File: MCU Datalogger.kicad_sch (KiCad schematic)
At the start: 25 parts, among them U1 24LC1025, U2 24LC1025, U3 ATMEGA328P-AU, U4 DS1337S_, Y1 Crystal, Y2 Crystal

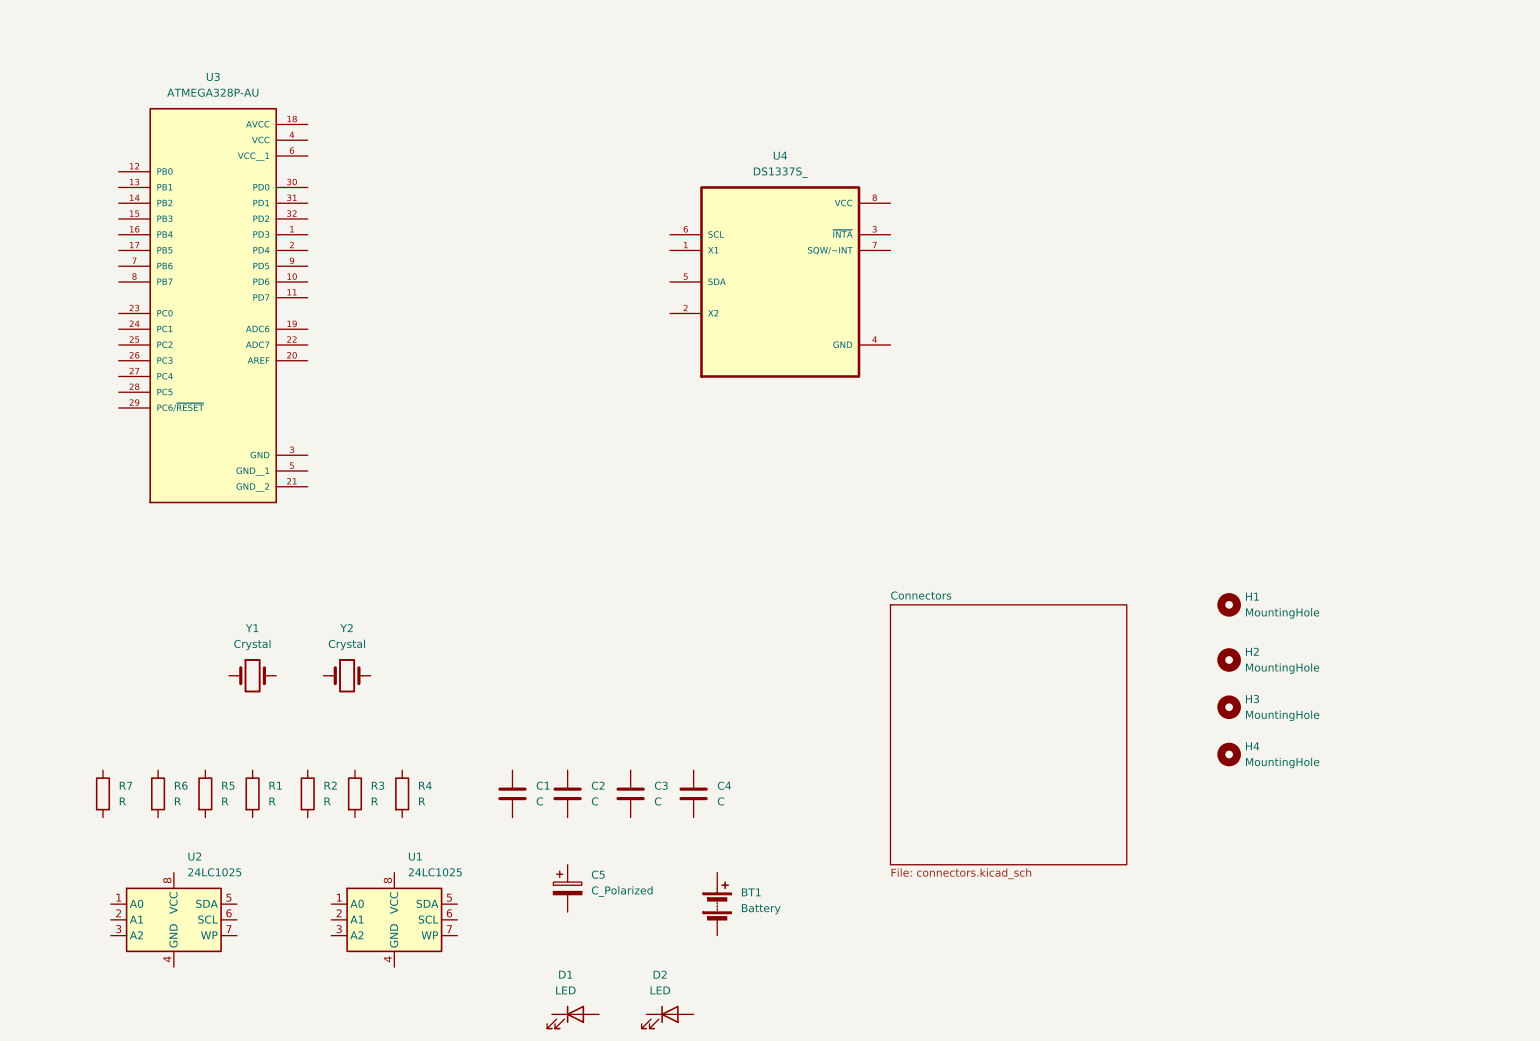
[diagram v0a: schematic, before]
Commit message: changed location of components
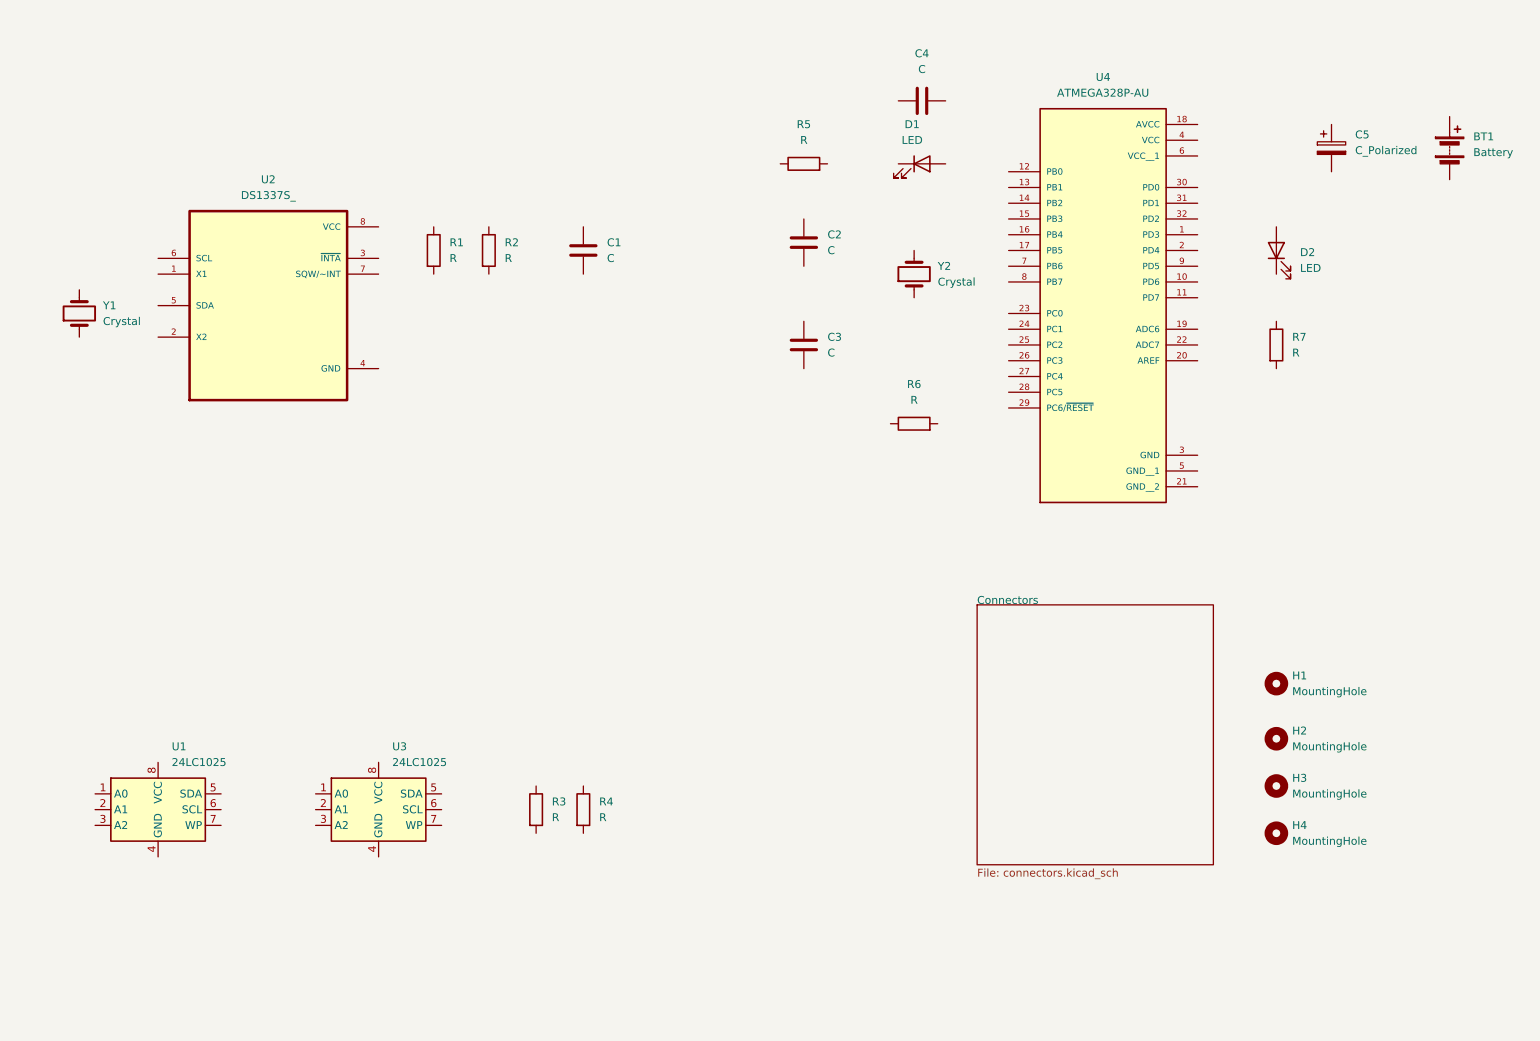
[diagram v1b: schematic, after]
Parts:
- renumbered R6 to R3, R5 to R4, R3 to R5, R7 to R6, R4 to R7, U2 to U1, U4 to U2, U1 to U3, U3 to U4
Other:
- moved on the sheet: BT1, C1, C2, C3, C4, C5, D1, D2, H1, H2, H3, H4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

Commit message: added component values
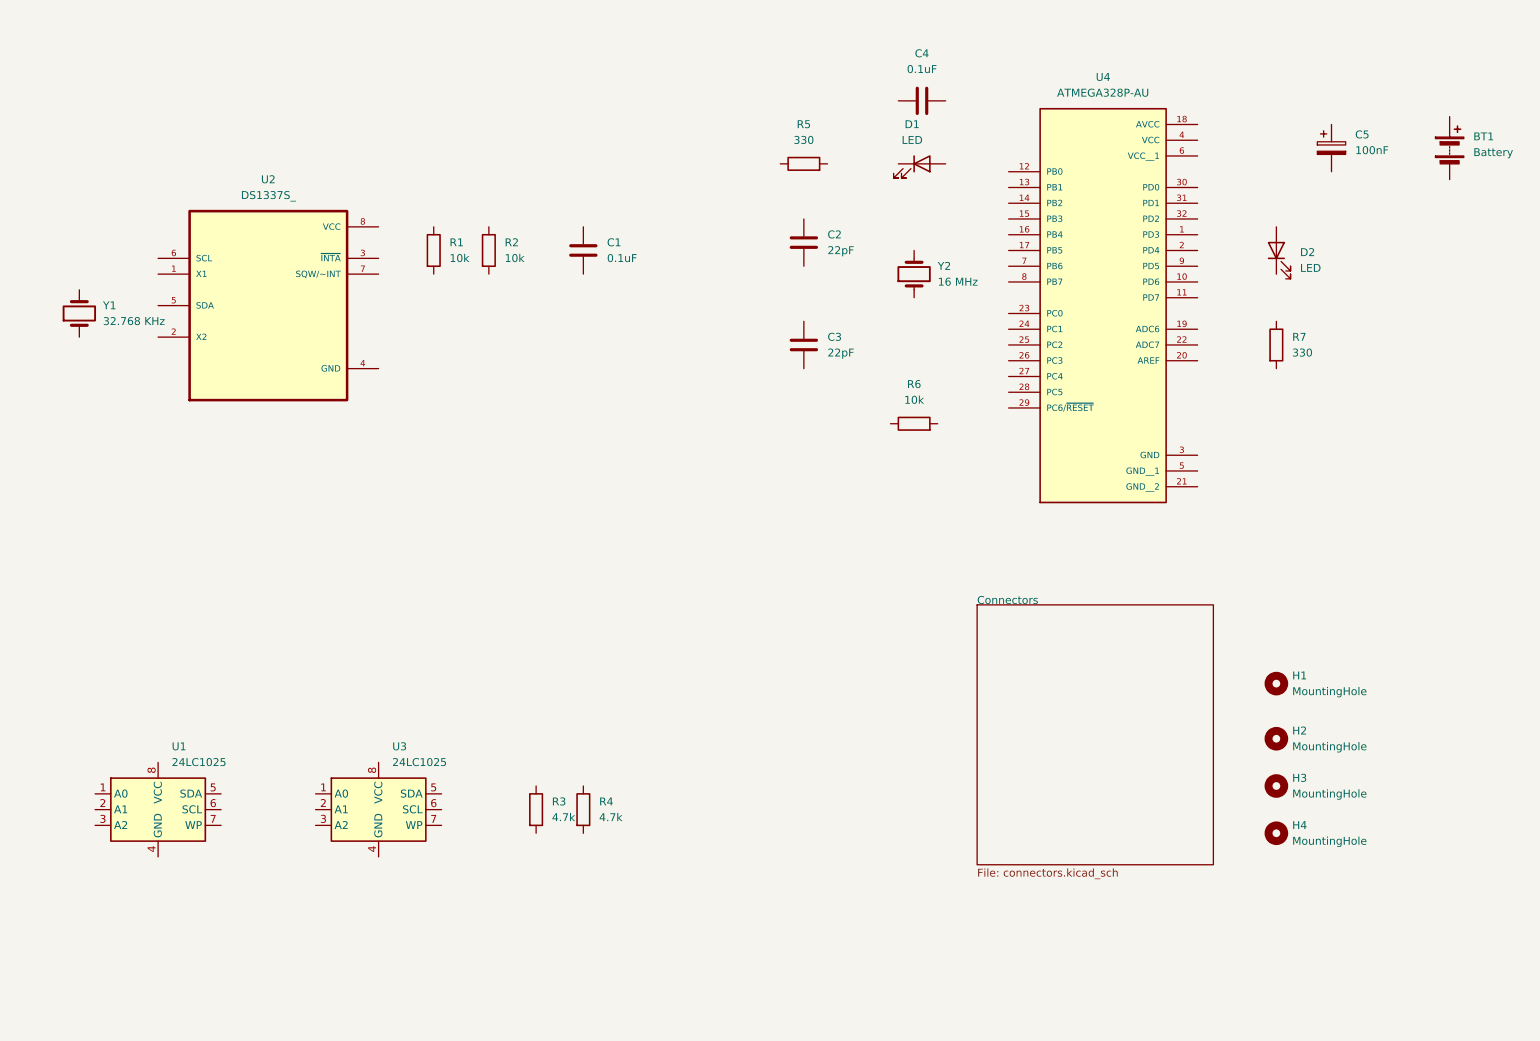
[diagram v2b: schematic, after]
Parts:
- C1, C4: value C -> 0.1uF
- C2, C3: value C -> 22pF
- C5: value C_Polarized -> 100nF
- R1, R2, R6: value R -> 10k
- R3, R4: value R -> 4.7k
- R5, R7: value R -> 330
- Y1: value Crystal -> 32.768 KHz
- Y2: value Crystal -> 16 MHz
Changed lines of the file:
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@@
 			)
 		)
-		(property "Value" "C"
+		(property "Value" "22pF"
 			(at 160.02 73.6599 0)
 			(effects
@@
 			)
 		)
-		(property "Value" "C"
+		(property "Value" "0.1uF"
 			(at 124.46 58.4199 0)
 			(effects
@@
 			)
 		)
-		(property "Value" "Crystal"
+		(property "Value" "32.768 KHz"
 			(at 43.18 68.5799 90)
 			(effects
@@
 			)
 		)
+		(property "Purpose" ""
+			(at 39.37 67.31 0)
+			(effects
+				(font
+					(size 1.27 1.27)
+				)
+				(hide yes)
+			)
+		)
 		(pin "2"
 		)
@@
 			)
 		)
-		(property "Value" "R"
+		(property "Value" "330"
 			(at 156.21 39.37 90)
 			(effects
@@
 			)
 		)
+		(property "Purpose" ""
+			(at 156.21 43.18 0)
+			(effects
+				(font
+					(size 1.27 1.27)
+				)
+				(hide yes)
+			)
+		)
 		(pin "2"
 		)
@@
 			)
 		)
-		(property "Value" "R"
+		(property "Value" "330"
 			(at 234.95 73.6599 0)
 			(effects
@@
 			)
 		)
-		(property "Value" "R"
+		(property "Value" "10k"
 			(at 107.95 58.4199 0)
 			(effects
@@
 			)
 		)
-		(property "Value" "C_Polarized"
+		(property "Value" "100nF"
 			(at 245.11 41.0209 0)
 			(effects
@@
 			)
 		)
-		(property "Value" "R"
+		(property "Value" "10k"
 			(at 99.06 58.4199 0)
 			(effects
@@
 			)
 		)
+		(property "Purpose" ""
+			(at 96.52 57.15 0)
+			(effects
+				(font
+					(size 1.27 1.27)
+				)
+				(hide yes)
+			)
+		)
 		(pin "2"
 		)
@@
 			)
 		)
-		(property "Value" "R"
+		(property "Value" "4.7k"
 			(at 115.57 148.5899 0)
 			(effects
@@
 			)
 		)
-		(property "Value" "R"
+		(property "Value" "4.7k"
 			(at 123.19 148.5899 0)
 			(effects
@@
 			)
 		)
-		(property "Value" "R"
+		(property "Value" "10k"
 			(at 173.99 81.28 90)
 			(effects
@@
 			)
 		)
-		(property "Value" "C"
+		(property "Value" "0.1uF"
 			(at 175.26 27.94 90)
 			(effects
@@
 			)
 		)
+		(property "Purpose" ""
+			(at 175.26 33.02 0)
+			(effects
+				(font
+					(size 1.27 1.27)
+				)
+				(hide yes)
+			)
+		)
 		(pin "2"
 		)
@@
 			)
 		)
-		(property "Value" "C"
+		(property "Value" "22pF"
 			(at 160.02 57.1499 0)
 			(effects
@@
 			)
 		)
-		(property "Value" "Crystal"
+		(property "Value" "16 MHz"
 			(at 177.8 62.2299 90)
 			(effects

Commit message: Added 3rd party footprints
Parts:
- BT1: footprint (none) -> Connector_PinHeader_1.00mm:PinHeader_1x02_P1.00mm_Vertical
- C1, C2, C3, C4, C5: footprint (none) -> Capacitor_SMD:C_0805_2012Metric_Pad1.18x1.45mm_HandSolder
- D1, D2: footprint (none) -> LED_SMD:LED_0805_2012Metric_Pad1.15x1.40mm_HandSolder
- H1, H2, H3, H4: footprint (none) -> MountingHole:MountingHole_2.1mm
- R1, R2, R3, R4, R5, R6, R7: footprint (none) -> Resistor_SMD:R_0805_2012Metric_Pad1.20x1.40mm_HandSolder
- U1, U3: footprint (none) -> Package_SO:SOIC-8_5.23x5.23mm_P1.27mm
- U2: footprint DS1337S_:SOIC127P600X175-8N -> footprints:SOIC127P600X175-8N
- U4: footprint ATMEGA328P-AU:QFP80P900X900X120-32N -> footprints:QFP80P900X900X120-32N
- Y1, Y2: footprint (none) -> Crystal:Crystal_SMD_5032-2Pin_5.0x3.2mm_HandSoldering
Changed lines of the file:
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@@
 			)
 		)
-		(property "Footprint" ""
+		(property "Footprint" "Capacitor_SMD:C_0805_2012Metric_Pad1.18x1.45mm_HandSolder"
 			(at 157.1752 76.2 0)
 			(effects
@@
 			)
 		)
-		(property "Footprint" ""
+		(property "Footprint" "Package_SO:SOIC-8_5.23x5.23mm_P1.27mm"
 			(at 87.63 147.32 0)
 			(effects
@@
 			)
 		)
-		(property "Footprint" ""
+		(property "Footprint" "Connector_PinHeader_1.00mm:PinHeader_1x02_P1.00mm_Vertical"
 			(at 260.35 39.116 90)
 			(effects
@@
 			)
 		)
-		(property "Footprint" ""
+		(property "Footprint" "MountingHole:MountingHole_2.1mm"
 			(at 232.41 135.89 0)
 			(effects
@@
 			)
 		)
-		(property "Footprint" ""
+		(property "Footprint" "MountingHole:MountingHole_2.1mm"
 			(at 232.41 127 0)
 			(effects
@@
 			)
 		)
-		(property "Footprint" ""
+		(property "Footprint" "Capacitor_SMD:C_0805_2012Metric_Pad1.18x1.45mm_HandSolder"
 			(at 121.6152 60.96 0)
 			(effects
@@
 			)
 		)
-		(property "Footprint" ""
+		(property "Footprint" "Crystal:Crystal_SMD_5032-2Pin_5.0x3.2mm_HandSoldering"
 			(at 39.37 67.31 0)
 			(effects
@@
 			)
 		)
-		(property "Footprint" ""
+		(property "Footprint" "Resistor_SMD:R_0805_2012Metric_Pad1.20x1.40mm_HandSolder"
 			(at 156.21 44.958 90)
 			(effects
@@
 			)
 		)
-		(property "Footprint" ""
+		(property "Footprint" "Resistor_SMD:R_0805_2012Metric_Pad1.20x1.40mm_HandSolder"
 			(at 230.632 72.39 90)
 			(effects
@@
 			)
 		)
-		(property "Footprint" ""
+		(property "Footprint" "Resistor_SMD:R_0805_2012Metric_Pad1.20x1.40mm_HandSolder"
 			(at 103.632 57.15 90)
 			(effects
@@
 			)
 		)
-		(property "Footprint" ""
+		(property "Footprint" "Capacitor_SMD:C_0805_2012Metric_Pad1.18x1.45mm_HandSolder"
 			(at 242.2652 44.45 0)
 			(effects
@@
 			)
 		)
-		(property "Footprint" ""
+		(property "Footprint" "Resistor_SMD:R_0805_2012Metric_Pad1.20x1.40mm_HandSolder"
 			(at 94.742 57.15 90)
 			(effects
@@
 			)
 		)
-		(property "Footprint" ""
+		(property "Footprint" "Resistor_SMD:R_0805_2012Metric_Pad1.20x1.40mm_HandSolder"
 			(at 111.252 147.32 90)
 			(effects
@@
 			)
 		)
-		(property "Footprint" ""
+		(property "Footprint" "Resistor_SMD:R_0805_2012Metric_Pad1.20x1.40mm_HandSolder"
 			(at 118.872 147.32 90)
 			(effects
@@
 			)
 		)
-		(property "Footprint" ""
+		(property "Footprint" "MountingHole:MountingHole_2.1mm"
 			(at 232.41 151.13 0)
 			(effects
@@
 			)
 		)
-		(property "Footprint" ""
+		(property "Footprint" "Resistor_SMD:R_0805_2012Metric_Pad1.20x1.40mm_HandSolder"
 			(at 173.99 86.868 90)
 			(effects
@@
 			)
 		)
-		(property "Footprint" ""
+		(property "Footprint" "LED_SMD:LED_0805_2012Metric_Pad1.15x1.40mm_HandSolder"
 			(at 232.41 57.15 0)
 			(effects
@@
 			)
 		)
-		(property "Footprint" ""
+		(property "Footprint" "Capacitor_SMD:C_0805_2012Metric_Pad1.18x1.45mm_HandSolder"
 			(at 179.07 32.0548 0)
 			(effects
@@
 			)
 		)
-		(property "Footprint" ""
+		(property "Footprint" "Package_SO:SOIC-8_5.23x5.23mm_P1.27mm"
 			(at 52.07 147.32 0)
 			(effects
@@
 			)
 		)
-		(property "Footprint" ""
+		(property "Footprint" "LED_SMD:LED_0805_2012Metric_Pad1.15x1.40mm_HandSolder"
 			(at 175.26 43.18 0)
 			(effects
@@
 			)
 		)
-		(property "Footprint" ""
+		(property "Footprint" "MountingHole:MountingHole_2.1mm"
 			(at 232.41 143.51 0)
 			(effects
@@
 			)
 		)
-		(property "Footprint" "DS1337S_:SOIC127P600X175-8N"
+		(property "Footprint" "footprints:SOIC127P600X175-8N"
 			(at 69.85 66.04 0)
 			(effects
@@
 			)
 		)
-		(property "Footprint" ""
+		(property "Footprint" "Capacitor_SMD:C_0805_2012Metric_Pad1.18x1.45mm_HandSolder"
 			(at 157.1752 59.69 0)
 			(effects
@@
 			)
 		)
-		(property "Footprint" "ATMEGA328P-AU:QFP80P900X900X120-32N"
+		(property "Footprint" "footprints:QFP80P900X900X120-32N"
 			(at 204.47 62.23 0)
 			(effects
@@
 			)
 		)
-		(property "Footprint" ""
+		(property "Footprint" "Crystal:Crystal_SMD_5032-2Pin_5.0x3.2mm_HandSoldering"
 			(at 173.99 60.96 0)
 			(effects

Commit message: Wired the main schematic
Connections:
- net GND: now reaches C3.1
- net GND: now also BT1.2 (-), C1.2, C2.1, C4.2, C5.2, R5.1, R7.2, U1.4 (GND), U1.7 (WP), U2.4 (GND), U3.2 (A1), U3.4 (GND), U3.7 (WP), U4.21 (GND__2), U4.3 (GND), U4.5 (GND__1)
- net at C3.2: now also U4.8 (PB7), Y2.1
- net Vcc: now reaches U3.1 (A0)
- net Vcc: now also C1.1, R1.1, R2.1, R3.1, R4.1, R6.1, U1.1 (A0), U1.2 (A1), U1.3 (A2), U1.8 (VCC), U2.8 (VCC), U3.3 (A2), U3.8 (VCC)
- net SDA: now reaches U3.5 (SDA)
- net SDA: now also R4.2, U1.5 (SDA), U2.5 (SDA), U4.27 (PC4)
- net SCL: now reaches U3.6 (SCL)
- net SCL: now also D1.2 (A), R3.2, U1.6 (SCL), U2.6 (SCL), U4.17 (PB5), U4.28 (PC5)
- net at BT1.1 (+): now also C5.1, D2.2 (A), U4.18 (AVCC), U4.4 (VCC)
- net at Y1.1: now also U2.2 (X2)
- net at Y1.2: now also U2.1 (X1)
- net at R5.2: now also D1.1 (K)
- net at R7.1: now also D2.1 (K)
- net at R2.2: now also U2.7 (SQW/~INT)
- net at R1.2: now also U2.3 (~{INTA})
- net RESET: now reaches R6.2
- net RESET: now also U4.29 (PC6/~{RESET})
- net at C4.1: now also U4.20 (AREF)
- net at C2.2: now also U4.7 (PB6), Y2.2
- net D3: now reaches U4.1 (PD3)
- net D6: now reaches U4.10 (PD6)
- net D7: now reaches U4.11 (PD7)
- net D8: now reaches U4.12 (PB0)
- net MOSI: now reaches U4.15 (PB3)
- net MISO: now reaches U4.16 (PB4)
- net D4: now reaches U4.2 (PD4)
- net RX: now reaches U4.30 (PD0)
- net TX: now reaches U4.31 (PD1)
- net D2: now reaches U4.32 (PD2)
- net D5: now reaches U4.9 (PD5)
- no-connect marks 0 -> 9
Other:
- moved on the sheet: BT1, C1, C2, C3, C4, C5, D2, R1, R2, R6, R7, Y2

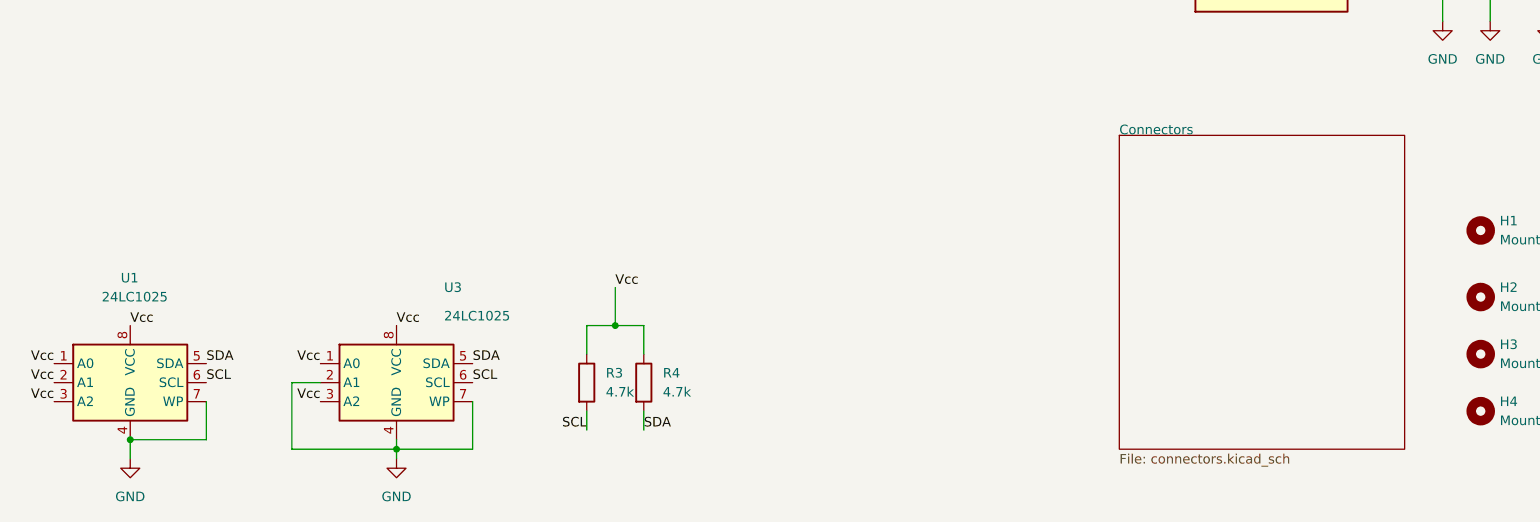
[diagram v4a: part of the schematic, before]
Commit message: Wired connectors sheet
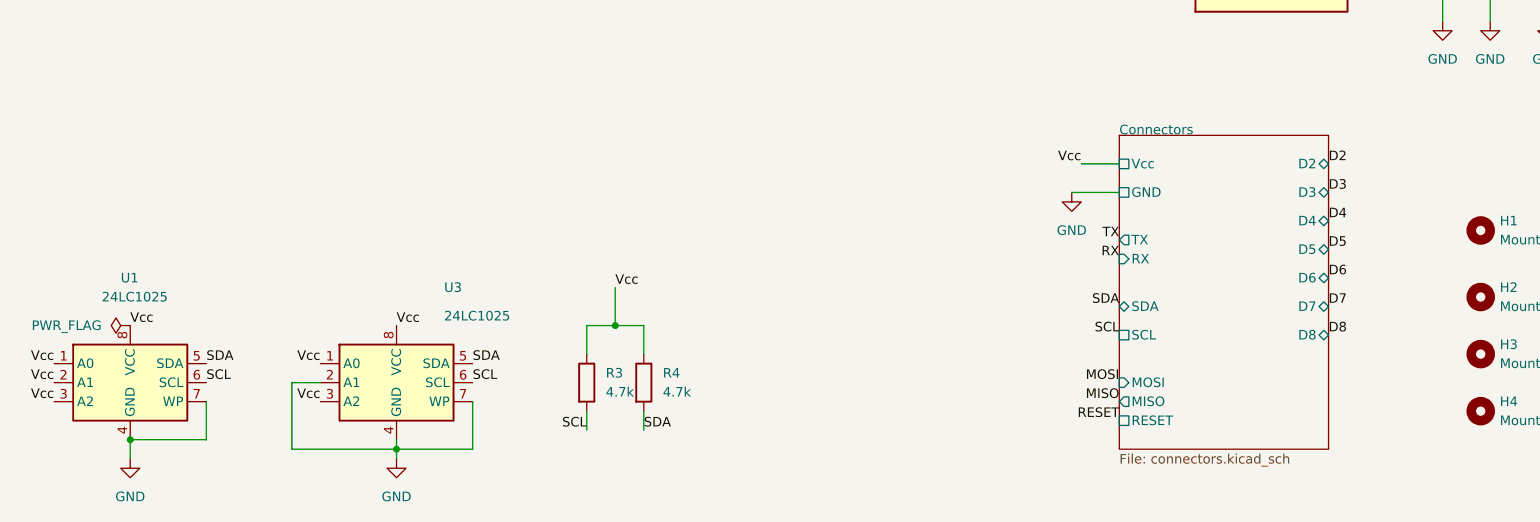
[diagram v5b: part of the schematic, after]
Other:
- sheet Connectors ports: added D2, D3, D4, D5, D6, D7, D8, GND, MISO, MOSI, RESET, RX, SCL, SDA, TX, Vcc; removed none
